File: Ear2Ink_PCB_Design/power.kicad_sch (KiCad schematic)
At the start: 1 part, among them U2 TPS562208DDCR

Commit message: added buck
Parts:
- added C11: 100nF, symbol Device:C
- added C12: 22uF, symbol Device:C
- added C13: 10uF, symbol Device:C
- added L1: L, symbol Device:L
- added R1: 56.2k, symbol Device:R_US
- added R2: 10k, symbol Device:R_US
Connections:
- net GND: now reaches U2.1 (GND)
- net GND: now also C12.2, C13.1, R2.2
- net at U2.2 (SW): now also C11.2, L1.1
- net 9V: now reaches U2.3 (VIN)
- net 9V: now also U2.5 (EN), C13.2
- net at U2.4 (VFB): now also R1.2, R2.1
- net at U2.6 (VBST): now also C11.1
- new net 5V: C12.1, L1.2, R1.1

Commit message: added some stuff
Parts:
- added C16, C17: C, symbol Device:C
- added U3: AZ1117-3.3, symbol Regulator_Linear:AZ1117-3.3
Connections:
- net 5V: now also C16.1, U3.3 (VI)
- net GND: now also C16.2, C17.2, U3.1 (GND)
- new net 3.3V: C17.1, U3.2 (VO)
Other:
- moved on the sheet: C11, C12, C13, L1, R1, R2, U2

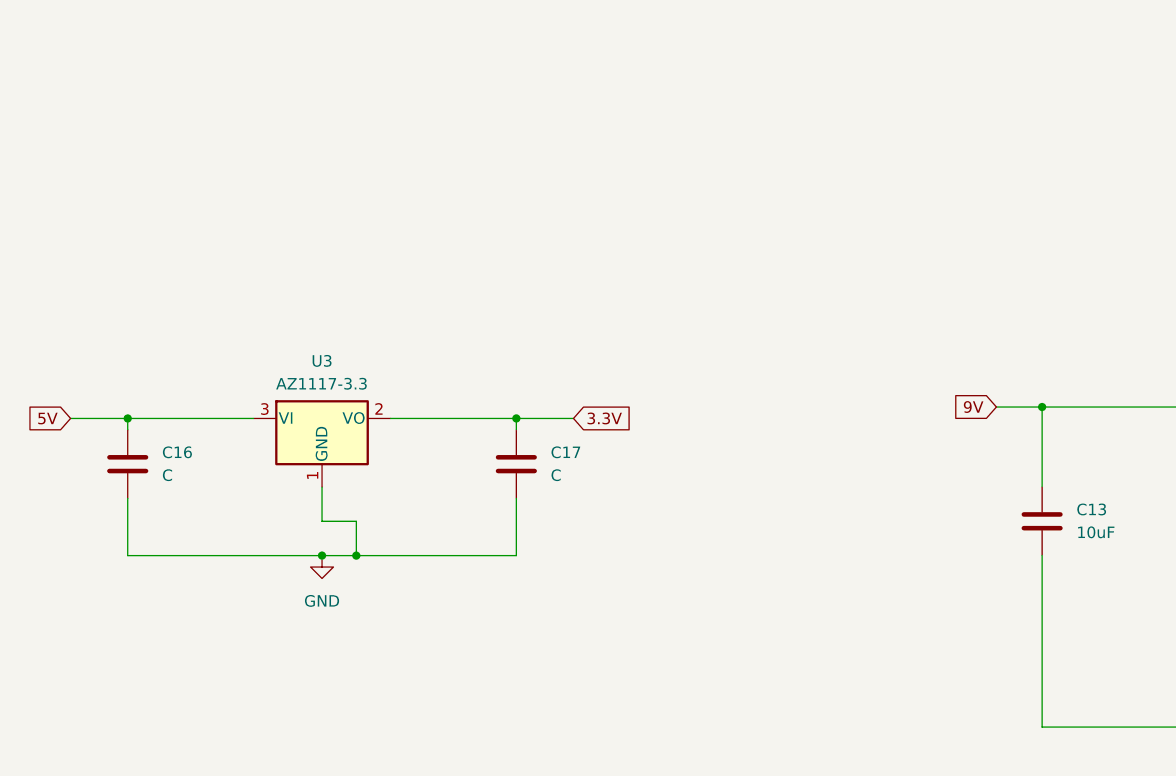
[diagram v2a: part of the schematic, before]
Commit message: added voltage prot
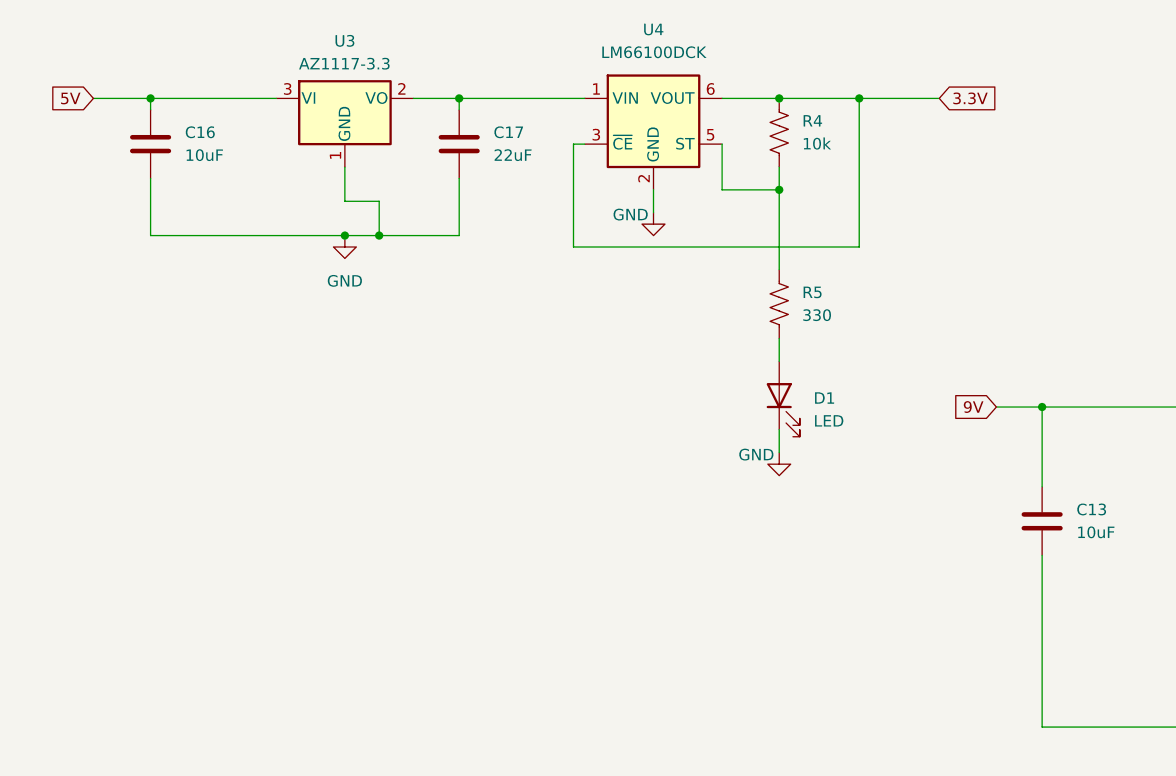
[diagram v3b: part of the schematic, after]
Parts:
- added D1: LED, symbol Device:LED
- added R4: 10k, symbol Device:R_US
- added R5: 330, symbol Device:R_US
- added U4: LM66100DCK, Package_TO_SOT_SMD:SOT-363_SC-70-6, symbol Power_Management:LM66100DCK
- C16: value C -> 10uF
- C17: value C -> 22uF
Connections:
- net 3.3V: now also R4.1, U4.3 (~{CE}), U4.6 (VOUT); no longer C17.1, U3.2 (VO)
- net GND: now also D1.1 (K), U4.2 (GND)
- new net: D1.2 (A), R5.2
- new net: R4.2, R5.1, U4.5 (ST)
- new net: C17.1, U3.2 (VO), U4.1 (VIN)
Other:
- moved on the sheet: C16, C17, U3

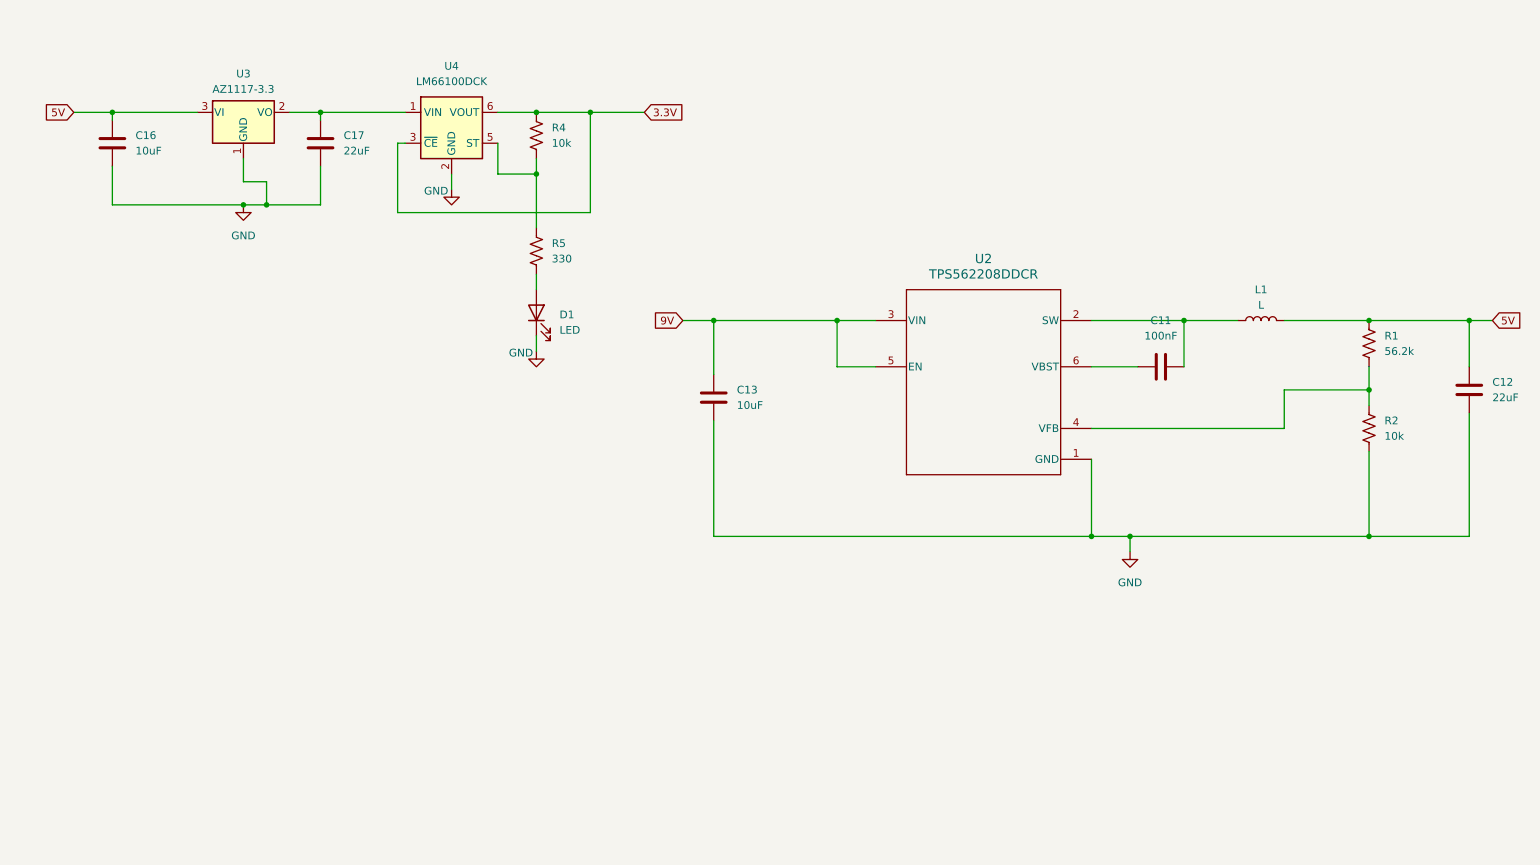
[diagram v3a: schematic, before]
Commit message: wired LCD and keypad
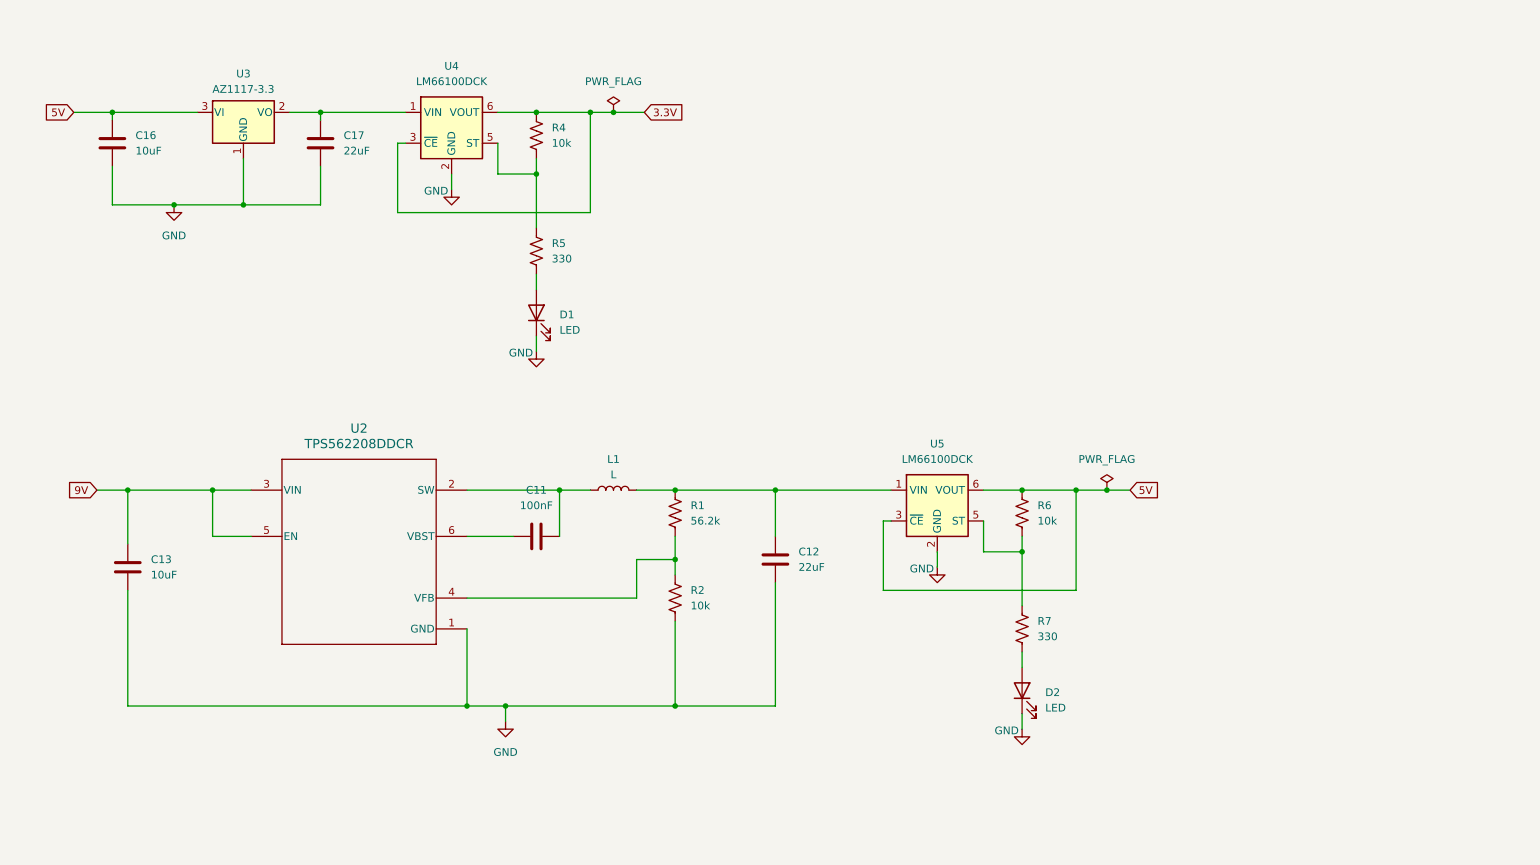
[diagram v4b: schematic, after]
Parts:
- added D2: LED, symbol Device:LED
- added R6: 10k, symbol Device:R_US
- added R7: 330, symbol Device:R_US
- added U5: LM66100DCK, Package_TO_SOT_SMD:SOT-363_SC-70-6, symbol Power_Management:LM66100DCK
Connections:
- net 5V: now also R6.1, U5.3 (~{CE}), U5.6 (VOUT); no longer C12.1, L1.2, R1.1
- net GND: now also D2.1 (K), U5.2 (GND)
- new net: R6.2, R7.1, U5.5 (ST)
- new net: C12.1, L1.2, R1.1, U5.1 (VIN)
- new net: D2.2 (A), R7.2
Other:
- moved on the sheet: C11, C12, C13, L1, R1, R2, U2

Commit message: started assigning footprints
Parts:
- R1, R2, R4, R5, R6, R7: footprint (none) -> Capacitor_SMD:C_0603_1608Metric_Pad1.08x0.95mm_HandSolder
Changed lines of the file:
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@@
 			)
 		)
-		(property "Footprint" ""
+		(property "Footprint" "Capacitor_SMD:C_0603_1608Metric_Pad1.08x0.95mm_HandSolder"
 			(at 190.246 105.664 90)
 			(effects
@@
 			)
 		)
-		(property "Footprint" ""
+		(property "Footprint" "Capacitor_SMD:C_0603_1608Metric_Pad1.08x0.95mm_HandSolder"
 			(at 133.096 105.664 90)
 			(effects
@@
 			)
 		)
-		(property "Footprint" ""
+		(property "Footprint" "Capacitor_SMD:C_0603_1608Metric_Pad1.08x0.95mm_HandSolder"
 			(at 190.246 124.714 90)
 			(effects
@@
 			)
 		)
-		(property "Footprint" ""
+		(property "Footprint" "Capacitor_SMD:C_0603_1608Metric_Pad1.08x0.95mm_HandSolder"
 			(at 110.236 43.434 90)
 			(effects
@@
 			)
 		)
-		(property "Footprint" ""
+		(property "Footprint" "Capacitor_SMD:C_0603_1608Metric_Pad1.08x0.95mm_HandSolder"
 			(at 133.096 119.634 90)
 			(effects
@@
 			)
 		)
-		(property "Footprint" ""
+		(property "Footprint" "Capacitor_SMD:C_0603_1608Metric_Pad1.08x0.95mm_HandSolder"
 			(at 110.236 62.484 90)
 			(effects

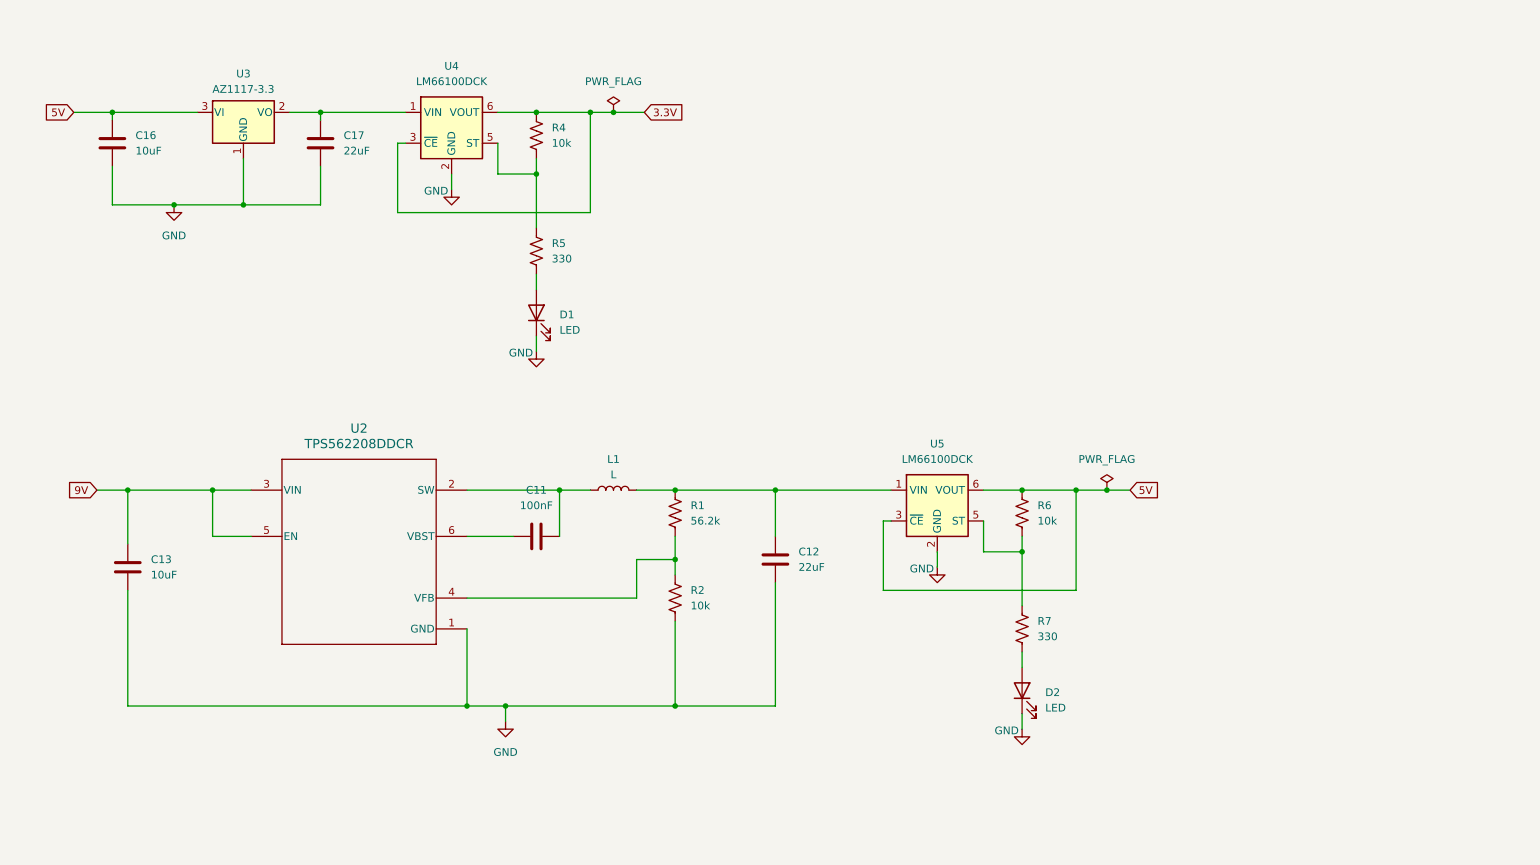
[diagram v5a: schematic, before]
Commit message: added esd prot and programming header
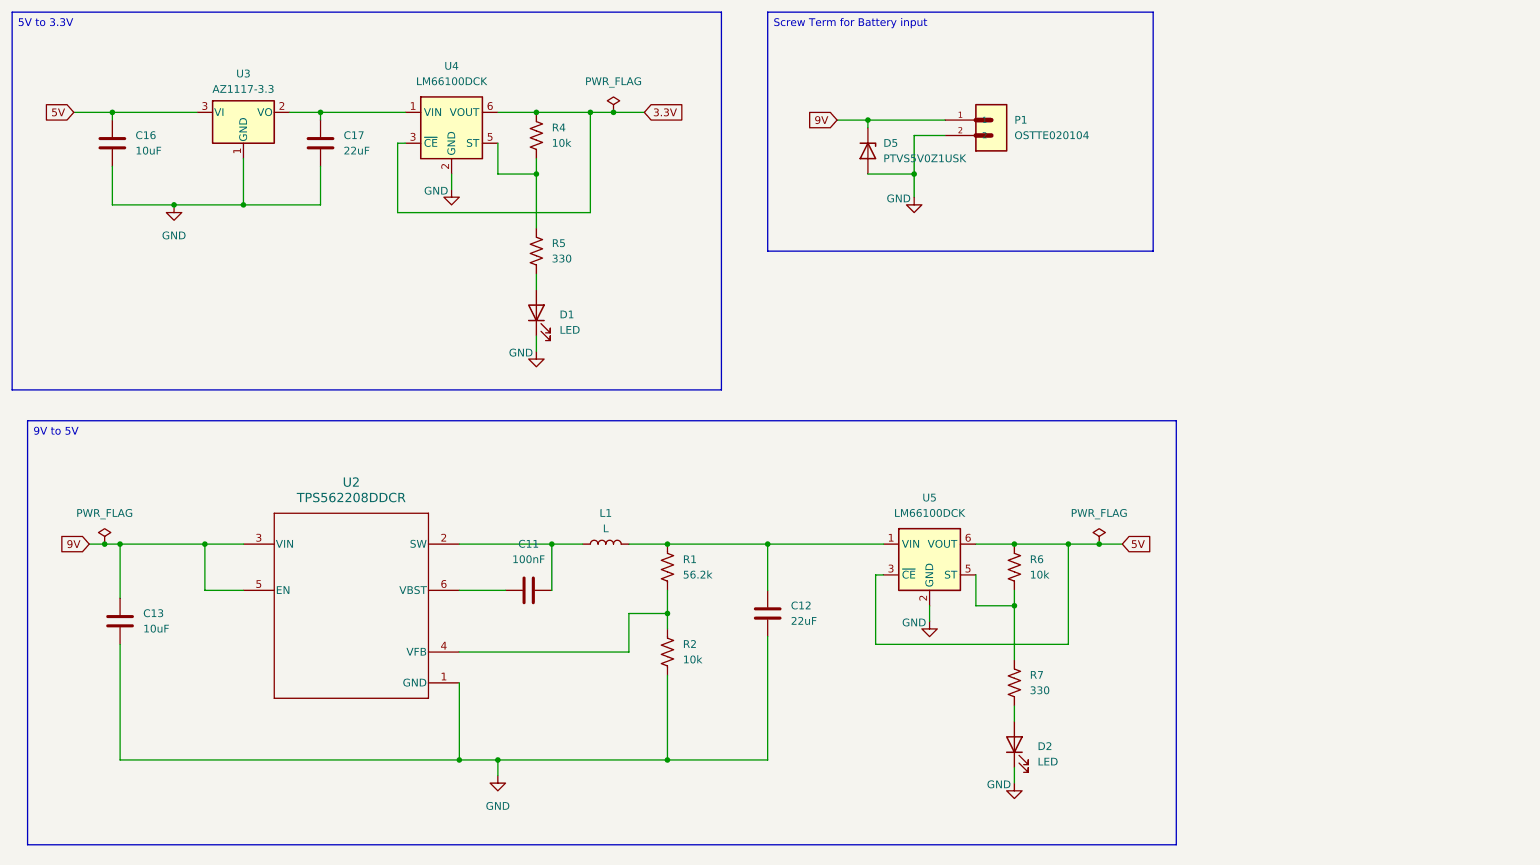
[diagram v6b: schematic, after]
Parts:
- added D5: PTVS5V0Z1USK, Diode_SMD:Nexperia_DSN1608-2_1.6x0.8mm, symbol Diode:PTVS5V0Z1USK
- added P1: OSTTE020104, OSTTE020104:OST_OSTTE020104, symbol OSTTE020104:OSTTE020104
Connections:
- net 9V: now also D5.1 (K), P1.1
- net GND: now also D5.2 (A), P1.2
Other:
- moved on the sheet: C11, C12, C13, D2, L1, R1, R2, R6, R7, U2, U5

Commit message: footprints
missing L tho
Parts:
- C11, C12, C13, C16, C17: footprint (none) -> Capacitor_SMD:C_0603_1608Metric_Pad1.08x0.95mm_HandSolder
- D1, D2: footprint (none) -> Resistor_SMD:R_0805_2012Metric_Pad1.20x1.40mm_HandSolder
- U2: footprint DDC0006A_N -> Buck:DDC0006A_N
- U3: footprint (none) -> LDO:SOT-223_DIO
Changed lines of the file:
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@@
 			)
 		)
-		(property "Footprint" ""
+		(property "Footprint" "Capacitor_SMD:C_0603_1608Metric_Pad1.08x0.95mm_HandSolder"
 			(at 111.76 117.1448 0)
 			(effects
@@
 			)
 		)
-		(property "Footprint" ""
+		(property "Footprint" "Resistor_SMD:R_0805_2012Metric_Pad1.20x1.40mm_HandSolder"
 			(at 109.22 72.39 0)
 			(effects
@@
 			)
 		)
-		(property "Footprint" ""
+		(property "Footprint" "Capacitor_SMD:C_0603_1608Metric_Pad1.08x0.95mm_HandSolder"
 			(at 74.6252 48.26 0)
 			(effects
@@
 			)
 		)
-		(property "Footprint" ""
+		(property "Footprint" "Resistor_SMD:R_0805_2012Metric_Pad1.20x1.40mm_HandSolder"
 			(at 187.96 143.51 0)
 			(effects
@@
 			)
 		)
-		(property "Footprint" "DDC0006A_N"
+		(property "Footprint" "Buck:DDC0006A_N"
 			(at 78.74 120.65 0)
 			(effects
@@
 			)
 		)
-		(property "Footprint" ""
+		(property "Footprint" "LDO:SOT-223_DIO"
 			(at 60.96 33.02 0)
 			(effects
@@
 			)
 		)
-		(property "Footprint" ""
+		(property "Footprint" "Capacitor_SMD:C_0603_1608Metric_Pad1.08x0.95mm_HandSolder"
 			(at 148.2852 125.73 0)
 			(effects
@@
 			)
 		)
-		(property "Footprint" ""
+		(property "Footprint" "Capacitor_SMD:C_0603_1608Metric_Pad1.08x0.95mm_HandSolder"
 			(at 40.3352 48.26 0)
 			(effects
@@
 			)
 		)
-		(property "Footprint" ""
+		(property "Footprint" "Capacitor_SMD:C_0603_1608Metric_Pad1.08x0.95mm_HandSolder"
 			(at 39.6748 119.38 0)
 			(effects

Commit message: all footprints done
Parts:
- removed L1: L, symbol Device:L
- added L1: IFSC1515AHER4R7M01, Inductor_SMD:L_Vishay_IFSC-1515AH_4x4x1.8mm, symbol Inductor:IFSC1515AHER4R7M01
- R1: value 56.2k -> 60k
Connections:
- net at C11.2, U2.2 (SW): now also L1.2
- net at C12.1, R1.1, U5.1 (VIN): now also L1.1
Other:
- moved on the sheet: C12, D2, R1, R2, R6, R7, U5
